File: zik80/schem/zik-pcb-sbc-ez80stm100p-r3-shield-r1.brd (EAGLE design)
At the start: 160 x 100 mm, 25 parts, among them IC1 TPS7133QP, U2 FT232RLSSOP

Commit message: shield progress.. about 50%? pcb coming together, working on placement. Schem has most or everything, just need to hook it all up.
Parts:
- removed PD0-TXD, PD1-RXD, USB3->PWR, USB5->PWR: (no value), pinhead:1X02
- removed X1: (no value), adafruit-musb-skeemod:4UCONN_20329
- removed X2: (no value), SparkFun-Connectors-skeemod:DB9
- added 3V3OUT, 5OUT, GNDOUT: (no value), pinhead:1X03
- added BOB-PA: (no value), pinhead:1X16
- added BOBGPIOB, GPIOC-JOY0, GPIOD-JOY1: (no value), pinhead:1X08
- added C23: 100uF, rcl:C025-025X050
- added C25: 250uF Pol, rcl:E3,5-8
- added C26: .05uF, rcl:C025-025X050
- added FT3V3->PWR3, FT5V->PWR5, LINEOUT, ZPD0-RXD, ZPD1-TXD: (no value), pinhead:1X02
- added JOY0, JOY1: (no value), SparkFun-Connectors-skeemod:DB9
- added PS2KEYB, PWRIN, SPKR: (no value), pinhead:1X04
- added R34: 1K, rcl:0204/7
- added R37: 10, rcl:0204/7
- added U$6: LM386-DIP, skeezix:LM386-DIP8
- added USBGPU, USBSERPWR: (no value), adafruit-musb-skeemod:4UCONN_20329
- added VGAHDR: (no value), pinhead:1X06
- moved PWROUT 146.8 mm to (12.7, 81.9), turned to 90 degrees
- moved U$1 146.5 mm to (141.0, 81.3)
- moved C3 144.9 mm to (80.0, 66.0)
- moved U$4 117.7 mm to (129.5, 33.0), turned to 270 degrees
- moved U$5 117.3 mm to (121.9, 101.6), turned to 270 degrees
- moved IC1 117.2 mm to (66.0, 54.6)
- moved U$2 109.7 mm to (129.5, 58.4), turned to 180 degrees
- moved USBPORT 109.3 mm to (22.9, 81.3), turned to 180 degrees
- moved SERSTATE 103.3 mm to (63.5, 66.0)
- moved CTSGND 99.8 mm to (49.5, 62.2)
- moved U$3 88.7 mm to (105.4, 87.6), turned to 270 degrees
- moved C1 81.7 mm to (33.0, 66.0)
- moved C2 81.7 mm to (39.4, 66.0)
- moved VGA1 80.0 mm to (81.3, 90.2), turned to 180 degrees
- moved R6 73.9 mm to (45.7, 27.9), turned to 180 degrees
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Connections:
- removed net +3V3: C3.2, IC1.5, IC1.6, IC1.7, PWROUT.3
- removed net PD0: PD0-TXD.2
- removed net PD1: PD1-RXD.2
- removed net PWR: USB3->PWR.2, USB5->PWR.2
- removed net VBUS: X1.VBUS
- new net N$1: C23.2, U$3.P$3
- new net N$2: U$3.P$1, U$6.3
- new net N$22: C25.+, C26.2, U$6.5
- new net N$23: C25.-
- new net N$24: C26.1, R37.2
- new net N$3: LINEOUT.2, U$6.7
- new net N$6: C23.1, R34.1, SPKR.1, SPKR.2, SPKR.3
- new net PWR3: 3V3OUT.1, 3V3OUT.2, 3V3OUT.3, C3.2, FT3V3->PWR3.2, IC1.5, IC1.6, IC1.7, PWRIN.3, PWROUT.3
- new net PWR5: 5OUT.1, 5OUT.2, 5OUT.3, FT5V->PWR5.2, IC1.3, IC1.4, PWRIN.2, PWROUT.2, U$1.CPIN
- new net SPA0: BOB-PA.1
- new net SPA10: BOB-PA.11
- new net SPA11: BOB-PA.12, USBGPU.D-
- new net SPA12: BOB-PA.13, USBGPU.D+
- new net ZPB0: BOBGPIOB.1
- new net ZPB2-SS: BOBGPIOB.3
- new net ZPB3-SCK: BOBGPIOB.4
- new net ZPB6-MISO: BOBGPIOB.7
- new net ZPB7-MOSI: BOBGPIOB.8
- new net ZPD0: GPIOD-JOY1.1, ZPD0-RXD.2
- new net ZPD1: GPIOD-JOY1.2, ZPD1-TXD.2
- new net ZPD6: GPIOD-JOY1.7
- new net ZPD7: GPIOD-JOY1.8
- net +5V: now also U$6.6, USBGPU.VBUS; no longer IC1.3, IC1.4, PWROUT.2
- net FTDI3: now also FT3V3->PWR3.1; no longer USB3->PWR.1
- net GND: now also GNDOUT.1, GNDOUT.2, GNDOUT.3, LINEOUT.1, PWRIN.4, R34.2, R37.1, U$3.P$2, U$6.2, U$6.4, USBGPU.BASE@1, USBGPU.BASE@2, USBGPU.GND, USBGPU.SPRT@1, USBGPU.SPRT@2, USBGPU.SPRT@3, USBGPU.SPRT@4, USBSERPWR.BASE@1, USBSERPWR.BASE@2, USBSERPWR.GND, USBSERPWR.SPRT@1, USBSERPWR.SPRT@2, USBSERPWR.SPRT@3, USBSERPWR.SPRT@4; no longer X1.BASE@1, X1.BASE@2, X1.GND, X1.SPRT@1, X1.SPRT@2, X1.SPRT@3, X1.SPRT@4
- net N$12: now also ZPD1-TXD.1; no longer PD0-TXD.1
- net N$13: now also ZPD0-RXD.1; no longer PD1-RXD.1
- net USB5: now also FT5V->PWR5.1, USBSERPWR.VBUS; no longer USB5->PWR.1
- net USB_D+: now also USBSERPWR.D-
- net USB_D-: now also USBSERPWR.D+
- net VCC: now also PWRIN.1; no longer U$1.CPIN
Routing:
- added copper zone on layer 16, net GND
- added copper zone on layer 1, net PWR3
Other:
- board size 160 x 100 mm -> 149.8 x 100.3 mm

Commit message: shield - Some placement progress
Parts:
- moved USBGPU 161.3 mm to (129.5, 95.2), turned to 180 degrees
- moved U$5 105.4 mm to (16.5, 100.3)
- moved U$4 103.6 mm to (50.8, 100.3), turned to 0 degrees
- moved JOY1 64.2 mm to (109.9, 79.4)
- moved U$3 23.3 mm to (114.3, 66.0)
- moved U$2 18.1 mm to (126.4, 40.6)
- moved USBPORT 16.9 mm to (8.89, 90.8)
- moved VGA1 14.7 mm to (76.8, 104.1)
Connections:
- net +5V: no longer USBGPU.VBUS
- net PWR5: now also USBGPU.VBUS
- net SPA11: now also USBGPU.D+; no longer USBGPU.D-
- net SPA12: now also USBGPU.D-; no longer USBGPU.D+
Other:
- outline, holes or cut-outs redrawn
- board text added: "Zikzak"

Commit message: Shield pcb rough layout coming together nicely
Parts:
- moved U$3 103.1 mm to (17.8, 102.2)
- moved 5OUT 84.5 mm to (83.2, 80.0)
- moved 3V3OUT 80.2 mm to (104.1, 80.0)
- moved GNDOUT 78.4 mm to (125.1, 80.0)
- moved U$5 61.9 mm to (-1.91, 41.3), turned to 0 degrees
- moved R37 59.1 mm to (128.9, 62.9), turned to 180 degrees
- moved C25 55.3 mm to (128.3, 68.6)
- moved ZPD1-TXD 52.1 mm to (66.0, 79.4)
- moved R34 43.9 mm to (99.7, 71.8), turned to 180 degrees
- moved ZPD0-RXD 41.5 mm to (54.6, 79.4)
- moved LINEOUT 40.3 mm to (128.3, 10.8)
- moved U$2 35.0 mm to (150.5, 15.2)
- moved RXLED 33.4 mm to (16.5, 11.4)
- moved U$6 28.4 mm to (109.9, 63.5)
- moved SERSTATE 24.8 mm to (39.4, 60.3)
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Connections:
- new net N$14: GPIOC-JOY0.4
- new net N$15: GPIOC-JOY0.5
- new net N$16: GPIOC-JOY0.6
- new net N$17: GPIOC-JOY0.7
- new net N$18: GPIOC-JOY0.8
- new net N$19: PS2KEYB.1
- new net N$20: PS2KEYB.2
- new net N$21: PS2KEYB.3
- new net N$25: PS2KEYB.4
- new net N$26: VGAHDR.1
- new net N$27: VGAHDR.2
- new net N$28: VGAHDR.3
- new net N$29: VGAHDR.4
- new net N$30: VGAHDR.5
- new net N$31: VGAHDR.6
- new net N$5: GPIOC-JOY0.1
- new net N$7: GPIOC-JOY0.2
- new net N$9: GPIOC-JOY0.3
- new net ZPD2: GPIOD-JOY1.3
- new net ZPD3: GPIOD-JOY1.4
- new net ZPD4: GPIOD-JOY1.5
- new net ZPD5: GPIOD-JOY1.6
- net GND: now also U$5.SG
- net N$23: now also U$5.R, U$5.T
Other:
- outline, holes or cut-outs redrawn
- board text added: "Zikshield for ZZr3 rev1 Jeff Mitchell 2016"

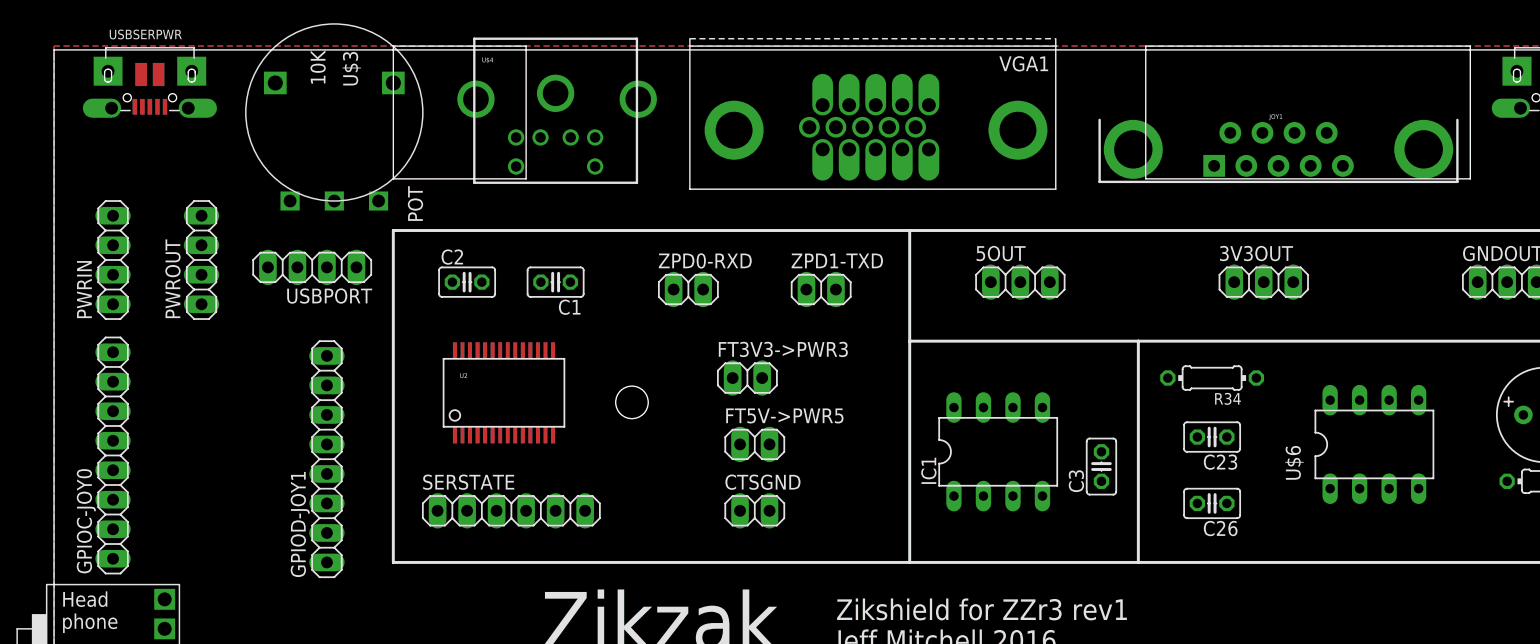
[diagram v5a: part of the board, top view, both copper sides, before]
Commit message: Working on the shield and proving jack layouts
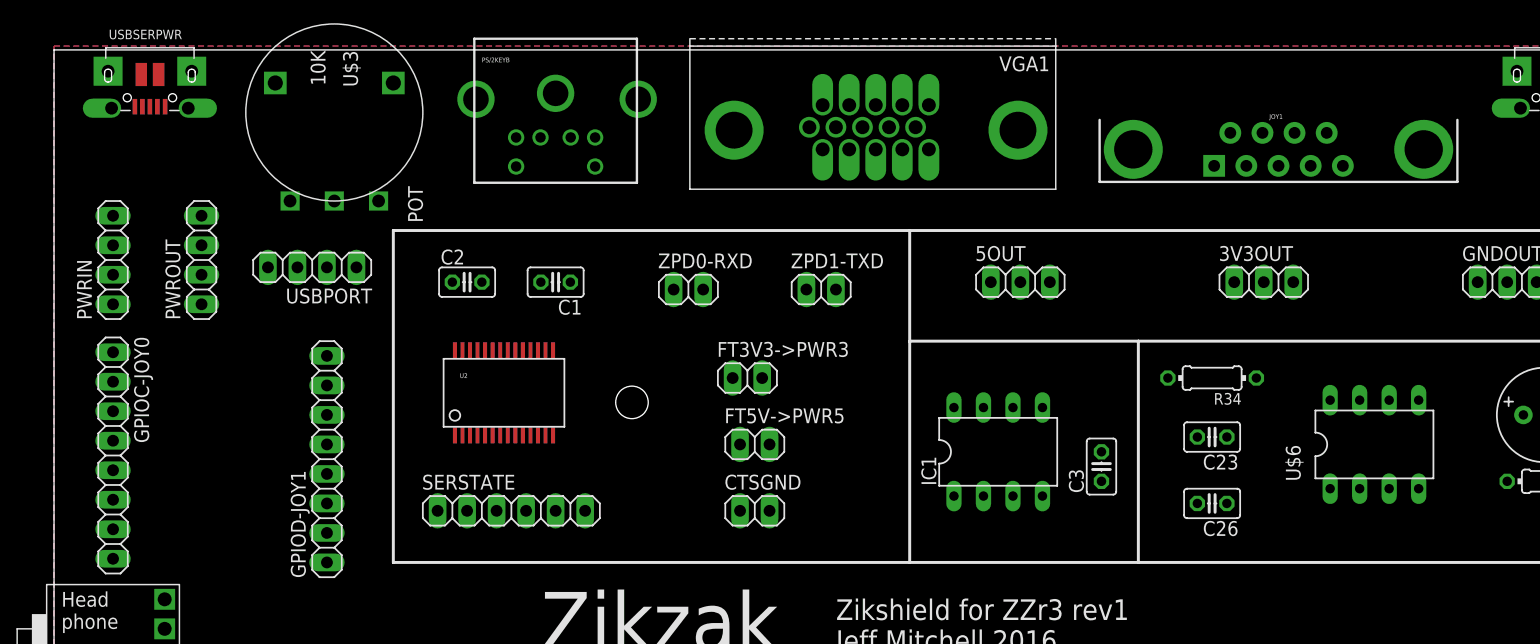
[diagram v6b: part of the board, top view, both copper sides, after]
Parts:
- turned GPIOC-JOY0 to 270 degrees
- renumbered U$4 to PS/2KEYB
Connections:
- net N$16 renamed ZPC5
- net N$17 renamed ZPC6
- net N$18 renamed ZPC7
- removed net N$14: GPIOC-JOY0.4
- removed net N$15: GPIOC-JOY0.5
- removed net N$19: PS2KEYB.1
- removed net N$20: PS2KEYB.2
- removed net N$21: PS2KEYB.3
- removed net N$25: PS2KEYB.4
- removed net N$5: GPIOC-JOY0.1
- removed net N$7: GPIOC-JOY0.2
- removed net N$9: GPIOC-JOY0.3
- new net ZPC0: GPIOC-JOY0.1, JOY0.5
- new net ZPC1: GPIOC-JOY0.2, JOY0.4
- new net ZPC2: GPIOC-JOY0.3, JOY0.3
- new net ZPC3: GPIOC-JOY0.4, JOY0.2
- new net ZPC4: GPIOC-JOY0.5, JOY0.9
- new net ZPD6_DATA: PS/2KEYB.1, PS2KEYB.4
- new net ZPD7_CLK: PS/2KEYB.5, PS2KEYB.1
- net GND: now also JOY0.7, PS/2KEYB.3, PS2KEYB.2, U$2.P8
- net PWR3: now also U$2.P6
- net PWR5: now also JOY0.8, PS/2KEYB.4, PS2KEYB.3
- net ZPB2-SS: now also BOB-PA.5, U$2.P4
- net ZPB3-SCK: now also BOB-PA.6, U$2.P7
- net ZPB6-MISO: now also BOB-PA.7, U$2.P9
- net ZPB7-MOSI: now also BOB-PA.8, U$2.P5
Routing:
- added copper zone on layer 1, net GND
- removed copper zone on layer 1, net PWR3
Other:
- board size 149.8 x 100.3 mm -> 149.8 x 100 mm
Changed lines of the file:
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@@
 <hole x="147.35175" y="96.29775" drill="2.8"/>
 <hole x="2.63525" y="10.19175" drill="2.8"/>
-<rectangle x1="29.21" y1="88.9" x2="40.64" y2="100.33" layer="46"/>
-<rectangle x1="93.98" y1="88.9" x2="121.92" y2="100.33" layer="46"/>
 <text x="41.91" y="48.26" size="5.08" layer="21">Zikzak</text>
 <wire x1="93.345" y1="74.93" x2="93.345" y2="55.88" width="0.254" layer="21"/>
@@
 <element name="U$2" library="skeezix" package="MICROSD10" value="MICROSD10" x="150.495" y="15.24" rot="R180"/>
 <element name="U$3" library="skeezix" package="POTWHEEL" value="10K" x="17.78" y="102.235" rot="R270"/>
-<element name="U$4" library="SparkFun-Connectors-skeemod" package="MINI-DIN6" value="MINI-DIN6PTH" x="43.18" y="100.965"/>
+<element name="PS/2KEYB" library="SparkFun-Connectors-skeemod" package="MINI-DIN6" value="MINI-DIN6PTH" x="43.18" y="100.965"/>
 <element name="JOY0" library="SparkFun-Connectors-skeemod" package="DB9" value="" x="8.255" y="24.765" rot="R90"/>
 <element name="VGA1" library="VideoConnectors-skeemod" package="DB-15-F90+SHIELD-BIG_PADS" value="VGA-F90B" x="70.485" y="104.775" rot="R180"/>
@@
 <element name="PWROUT" library="pinhead" package="1X04" value="" x="12.7" y="81.915" rot="R90"/>
 <element name="PWRIN" library="pinhead" package="1X04" value="" x="5.08" y="81.915" rot="R90"/>
-<element name="GPIOC-JOY0" library="pinhead" package="1X08" value="" x="5.08" y="65.0875" rot="R90"/>
+<element name="GPIOC-JOY0" library="pinhead" package="1X08" value="" x="5.08" y="65.0875" rot="R270"/>
 <element name="BOBGPIOB" library="pinhead" package="1X08" value="" x="13.97" y="5.08"/>
 <element name="GPIOD-JOY1" library="pinhead" package="1X08" value="" x="23.495" y="64.77" rot="R90"/>
@@
 <contactref element="USBGPU" pad="BASE@1"/>
 <contactref element="U$5" pad="SG"/>
+<contactref element="PS2KEYB" pad="2"/>
+<polygon width="0.4064" layer="1">
+<vertex x="0" y="0"/>
+<vertex x="0" y="100.33"/>
+<vertex x="149.86" y="100.33"/>
+<vertex x="149.86" y="0"/>
+</polygon>
+<contactref element="PS/2KEYB" pad="3"/>
+<contactref element="U$2" pad="P8"/>
+<contactref element="JOY0" pad="7"/>
 <wire x1="130.29" y1="97.885" x2="133.14" y2="98.166" width="0" layer="19" extent="1-1"/>
-<wire x1="128.79" y1="97.885" x2="130.29" y2="97.885" width="0" layer="19" extent="1-1"/>
 <wire x1="128.24" y1="95.11" x2="128.79" y2="97.885" width="0" layer="19" extent="1-1"/>
-<wire x1="126.24" y1="94.985" x2="128.24" y2="95.11" width="0" layer="19" extent="1-1"/>
-<wire x1="6.955" y1="95.11" x2="4.955" y2="94.985" width="0" layer="19" extent="1-1"/>
 <wire x1="7.505" y1="97.885" x2="6.955" y2="95.11" width="0" layer="19" extent="1-1"/>
-<wire x1="9.005" y1="97.885" x2="7.505" y2="97.885" width="0" layer="19" extent="1-1"/>
 <wire x1="125.94" y1="98.166" x2="128.79" y2="97.885" width="0" layer="19" extent="1-1"/>
 <wire x1="11.855" y1="98.166" x2="9.005" y2="97.885" width="0" layer="19" extent="1-1"/>
 <wire x1="4.655" y1="98.166" x2="7.505" y2="97.885" width="0" layer="19" extent="1-1"/>
-<wire x1="36.46" y1="74.141" x2="36.83" y2="80.01" width="0" layer="19" extent="1-1"/>
-<wire x1="35.81" y1="74.141" x2="36.46" y2="74.141" width="0" layer="19" extent="1-1"/>
-<wire x1="39.06" y1="74.141" x2="36.46" y2="74.141" width="0" layer="19" extent="1-1"/>
-<wire x1="41.01" y1="74.141" x2="39.06" y2="74.141" width="0" layer="19" extent="1-1"/>
-<wire x1="38.41" y1="66.829" x2="39.06" y2="74.141" width="0" layer="19" extent="1-1"/>
 </signal>
 <signal name="+5V">
@@
 <contactref element="3V3OUT" pad="2"/>
 <contactref element="3V3OUT" pad="3"/>
-<polygon width="0.4064" layer="1">
-<vertex x="0" y="0"/>
-<vertex x="0" y="100.33"/>
-<vertex x="149.86" y="100.33"/>
-<vertex x="149.86" y="0"/>
-</polygon>
+<contactref element="U$2" pad="P6"/>
+<wire x1="104.14" y1="80.01" x2="106.68" y2="80.01" width="0" layer="19" extent="1-1"/>
+<wire x1="101.6" y1="80.01" x2="104.14" y2="80.01" width="0" layer="19" extent="1-1"/>
+<wire x1="90.17" y1="65.405" x2="101.6" y2="80.01" width="0" layer="19" extent="1-1"/>
+<wire x1="85.09" y1="69.215" x2="90.17" y2="65.405" width="0" layer="19" extent="1-1"/>
+<wire x1="82.55" y1="69.215" x2="85.09" y2="69.215" width="0" layer="19" extent="1-1"/>
+<wire x1="80.01" y1="69.215" x2="82.55" y2="69.215" width="0" layer="19" extent="1-1"/>
+<wire x1="60.96" y1="71.755" x2="80.01" y2="69.215" width="0" layer="19" extent="1-1"/>
+<wire x1="12.7" y1="83.185" x2="60.96" y2="71.755" width="0" layer="19" extent="1-1"/>
+<wire x1="5.08" y1="83.185" x2="12.7" y2="83.185" width="0" layer="19" extent="1-1"/>
+<wire x1="138.2776" y1="8.0772" x2="90.17" y2="65.405" width="0" layer="19" extent="1-1"/>
 </signal>
 <signal name="USB5">
@@
 <contactref element="5OUT" pad="3"/>
 <contactref element="USBGPU" pad="VBUS"/>
+<contactref element="PS2KEYB" pad="3"/>
+<contactref element="PS/2KEYB" pad="4"/>
+<contactref element="JOY0" pad="8"/>
 <wire x1="130.84" y1="95.11" x2="142.24" y2="84.582" width="0" layer="19" extent="1-1"/>
 <wire x1="85.725" y1="80.01" x2="130.84" y2="95.11" width="0" layer="19" extent="1-1"/>
@@
 <wire x1="82.55" y1="61.595" x2="85.09" y2="61.595" width="0" layer="19" extent="1-1"/>
 <wire x1="61.595" y1="66.04" x2="82.55" y2="61.595" width="0" layer="19" extent="1-1"/>
-<wire x1="12.7" y1="80.645" x2="61.595" y2="66.04" width="0" layer="19" extent="1-1"/>
+<wire x1="46.58" y1="92.465" x2="61.595" y2="66.04" width="0" layer="19" extent="1-1"/>
+<wire x1="12.7" y1="80.645" x2="46.58" y2="92.465" width="0" layer="19" extent="1-1"/>
 <wire x1="5.08" y1="80.645" x2="12.7" y2="80.645" width="0" layer="19" extent="1-1"/>
+<wire x1="6.835" y1="26.145" x2="5.08" y2="80.645" width="0" layer="19" extent="1-1"/>
+<wire x1="132.08" y1="3.81" x2="85.09" y2="61.595" width="0" layer="19" extent="1-1"/>
 </signal>
 <signal name="ZPD0">
@@
 <signal name="ZPB2-SS">
 <contactref element="BOBGPIOB" pad="3"/>
+<contactref element="BOB-PA" pad="5"/>
+<contactref element="U$2" pad="P4"/>
+<wire x1="138.2776" y1="10.2108" x2="146.05" y2="27.94" width="0" layer="19" extent="1-1"/>
+<wire x1="10.16" y1="5.08" x2="138.2776" y2="10.2108" width="0" layer="19" extent="1-1"/>
 </signal>
 <signal name="ZPB3-SCK">
 <contactref element="BOBGPIOB" pad="4"/>
+<contactref element="BOB-PA" pad="6"/>
+<contactref element="U$2" pad="P7"/>
+<wire x1="138.2776" y1="7.0104" x2="146.05" y2="30.48" width="0" layer="19" extent="1-1"/>
+<wire x1="12.7" y1="5.08" x2="138.2776" y2="7.0104" width="0" layer="19" extent="1-1"/>
 </signal>
 <signal name="ZPB6-MISO">
 <contactref element="BOBGPIOB" pad="7"/>
+<contactref element="BOB-PA" pad="7"/>
+<contactref element="U$2" pad="P9"/>
+<wire x1="138.2776" y1="4.8768" x2="146.05" y2="33.02" width="0" layer="19" extent="1-1"/>
+<wire x1="20.32" y1="5.08" x2="138.2776" y2="4.8768" width="0" layer="19" extent="1-1"/>
 </signal>
 <signal name="ZPB7-MOSI">
 <contactref element="BOBGPIOB" pad="8"/>
+<contactref element="BOB-PA" pad="8"/>
+<contactref element="U$2" pad="P5"/>
+<wire x1="138.2776" y1="9.144" x2="146.05" y2="35.56" width="0" layer="19" extent="1-1"/>
+<wire x1="22.86" y1="5.08" x2="138.2776" y2="9.144" width="0" layer="19" extent="1-1"/>
 </signal>
 <signal name="SPA0">
@@
 <contactref element="GPIOD-JOY1" pad="6"/>
 </signal>
-<signal name="N$5">
+<signal name="ZPC0">
 <contactref element="GPIOC-JOY0" pad="1"/>
-</signal>
-<signal name="N$7">
+<contactref element="JOY0" pad="5"/>
+<wire x1="9.675" y1="30.305" x2="5.08" y2="73.9775" width="0" layer="19" extent="1-1"/>
+</signal>
+<signal name="ZPC1">
 <contactref element="GPIOC-JOY0" pad="2"/>
-</signal>
-<signal name="N$9">
+<contactref element="JOY0" pad="4"/>
+<wire x1="9.675" y1="27.535" x2="5.08" y2="71.4375" width="0" layer="19" extent="1-1"/>
+</signal>
+<signal name="ZPC2">
 <contactref element="GPIOC-JOY0" pad="3"/>
-</signal>
-<signal name="N$14">
+<contactref element="JOY0" pad="3"/>
+<wire x1="9.675" y1="24.765" x2="5.08" y2="68.8975" width="0" layer="19" extent="1-1"/>
+</signal>
+<signal name="ZPC3">
 <contactref element="GPIOC-JOY0" pad="4"/>
-</signal>
-<signal name="N$15">
+<contactref element="JOY0" pad="2"/>
+<wire x1="9.675" y1="21.995" x2="5.08" y2="66.3575" width="0" layer="19" extent="1-1"/>
+</signal>
+<signal name="ZPC4">
 <contactref element="GPIOC-JOY0" pad="5"/>
-</signal>
-<signal name="N$16">
+<contactref element="JOY0" pad="9"/>
+<wire x1="6.835" y1="28.915" x2="5.08" y2="63.8175" width="0" layer="19" extent="1-1"/>
+</signal>
+<signal name="ZPC5">
 <contactref element="GPIOC-JOY0" pad="6"/>
 </signal>
-<signal name="N$17">
+<signal name="ZPC6">
 <contactref element="GPIOC-JOY0" pad="7"/>
 </signal>
-<signal name="N$18">
+<signal name="ZPC7">
 <contactref element="GPIOC-JOY0" pad="8"/>
 </signal>
-<signal name="N$19">
-<contactref element="PS2KEYB" pad="1"/>
-</signal>
-<signal name="N$20">
-<contactref element="PS2KEYB" pad="2"/>
-</signal>
-<signal name="N$21">
-<contactref element="PS2KEYB" pad="3"/>
-</signal>
-<signal name="N$25">
+<signal name="ZPD6_DATA">
 <contactref element="PS2KEYB" pad="4"/>
+<contactref element="PS/2KEYB" pad="1"/>
+<wire x1="41.88" y1="92.465" x2="134.62" y2="3.81" width="0" layer="19" extent="1-1"/>
 </signal>
 <signal name="N$26">
@@
 <contactref element="VGAHDR" pad="6"/>
 </signal>
+<signal name="ZPD7_CLK">
+<contactref element="PS2KEYB" pad="1"/>
+<contactref element="PS/2KEYB" pad="5"/>
+<wire x1="39.78" y1="89.965" x2="127" y2="3.81" width="0" layer="19" extent="1-1"/>
+</signal>
 </signals>

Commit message: Shield incremental
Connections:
- net GND: now also JOY1.7
- net PWR5: now also JOY1.8
- net ZPD0: now also JOY1.5
- net ZPD1: now also JOY1.4
- net ZPD2: now also JOY1.3
- net ZPD3: now also JOY1.2
- net ZPD4: now also JOY1.9
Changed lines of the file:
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@@
 <contactref element="U$2" pad="P8"/>
 <contactref element="JOY0" pad="7"/>
+<contactref element="JOY1" pad="7"/>
 <wire x1="130.29" y1="97.885" x2="133.14" y2="98.166" width="0" layer="19" extent="1-1"/>
 <wire x1="128.24" y1="95.11" x2="128.79" y2="97.885" width="0" layer="19" extent="1-1"/>
@@
 <contactref element="PS/2KEYB" pad="4"/>
 <contactref element="JOY0" pad="8"/>
+<contactref element="JOY1" pad="8"/>
 <wire x1="130.84" y1="95.11" x2="142.24" y2="84.582" width="0" layer="19" extent="1-1"/>
-<wire x1="85.725" y1="80.01" x2="130.84" y2="95.11" width="0" layer="19" extent="1-1"/>
+<wire x1="106.79" y1="92.86" x2="130.84" y2="95.11" width="0" layer="19" extent="1-1"/>
+<wire x1="85.725" y1="80.01" x2="106.79" y2="92.86" width="0" layer="19" extent="1-1"/>
 <wire x1="83.185" y1="80.01" x2="85.725" y2="80.01" width="0" layer="19" extent="1-1"/>
 <wire x1="80.645" y1="80.01" x2="83.185" y2="80.01" width="0" layer="19" extent="1-1"/>
@@
 <contactref element="GPIOD-JOY1" pad="1"/>
 <contactref element="ZPD0-RXD" pad="2"/>
+<contactref element="JOY1" pad="5"/>
+<wire x1="55.88" y1="79.375" x2="110.95" y2="90.02" width="0" layer="19" extent="1-1"/>
 <wire x1="23.495" y1="55.88" x2="55.88" y2="79.375" width="0" layer="19" extent="1-1"/>
 </signal>
@@
 <contactref element="GPIOD-JOY1" pad="2"/>
 <contactref element="ZPD1-TXD" pad="2"/>
+<contactref element="JOY1" pad="4"/>
+<wire x1="67.31" y1="79.375" x2="108.18" y2="90.02" width="0" layer="19" extent="1-1"/>
 <wire x1="23.495" y1="58.42" x2="67.31" y2="79.375" width="0" layer="19" extent="1-1"/>
 </signal>
@@
 <signal name="ZPD2">
 <contactref element="GPIOD-JOY1" pad="3"/>
+<contactref element="JOY1" pad="3"/>
+<wire x1="23.495" y1="60.96" x2="105.41" y2="90.02" width="0" layer="19" extent="1-1"/>
 </signal>
 <signal name="ZPD3">
 <contactref element="GPIOD-JOY1" pad="4"/>
+<contactref element="JOY1" pad="2"/>
+<wire x1="23.495" y1="63.5" x2="102.64" y2="90.02" width="0" layer="19" extent="1-1"/>
 </signal>
 <signal name="ZPD4">
 <contactref element="GPIOD-JOY1" pad="5"/>
+<contactref element="JOY1" pad="9"/>
+<wire x1="23.495" y1="66.04" x2="109.56" y2="92.86" width="0" layer="19" extent="1-1"/>
 </signal>
 <signal name="ZPD5">
